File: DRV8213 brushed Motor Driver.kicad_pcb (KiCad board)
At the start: 4 copper layers, 15 x 15 mm, 26 parts, among them J1 Keystone 6102, J10 Precidip 852-10-004-20-001101, J11 Precidip 852-10-004-20-001101, J2 Keystone 6102, J3 Keystone 6100, J4 Keystone 6100, J5 Keystone 6102, J6 Keystone 6102, J7 Keystone 6100, J8 Keystone 6100, J9 JST PH 2mm horizontal, U1 DRV8213RTER, U2 LP2981-3.3

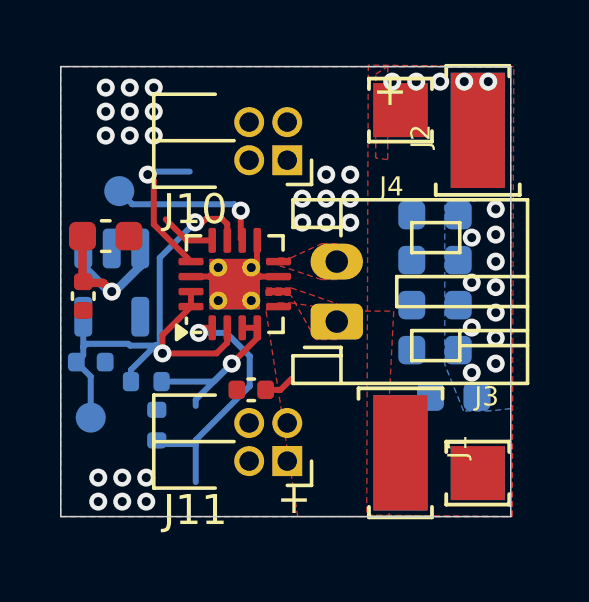
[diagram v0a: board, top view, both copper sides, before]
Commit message: Relayout with new components
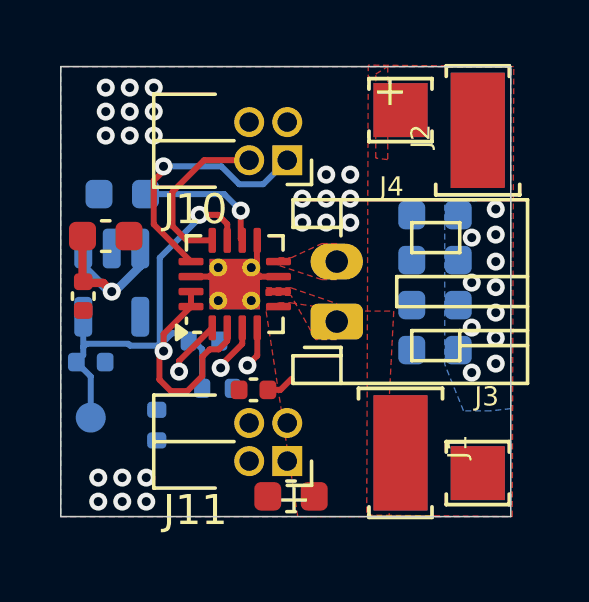
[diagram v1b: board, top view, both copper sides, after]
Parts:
- removed TP1: tinrush, TestPoint:TestPoint_Pad_D1.0mm
- added C10: 33nF, Capacitor_SMD:C_0603_1608Metric, B.Cu at (165.8, 98.5)
- added R3: 10k, Resistor_SMD:R_0402_1005Metric, B.Cu at (168.6, 103.3)
- C5: moved to F.Cu
- moved C5 6.36 mm to (171.5, 108.5)
- moved R1 2.39 mm to (169.0, 104.9)
- moved C6 0.07 mm to (170.2, 105.0)
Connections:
- J11 pad 2: ADC-A -> Stall
- R1 pad 2: Fault -> Stall
- U1 pad 3: Fault -> Stall
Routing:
- net ADC-A: track 8.94 -> 2.09 mm
- net Fault: track 6.54 -> 1.39 mm
- net PWM-B: track 1.84 -> 5.66 mm
- net +3.3V: track 19.8 -> 23.5 mm
- net PWM-A: track 4.94 -> 8.53 mm
- net Stall: track 0.00 -> 1.63 mm, vias 0 -> 1
- net Net-(U1-TINRUSH): track 5.33 -> 4.42 mm
- net VDD: track 7.51 -> 7.43 mm, vias 17 -> 12

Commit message: Finished reroute
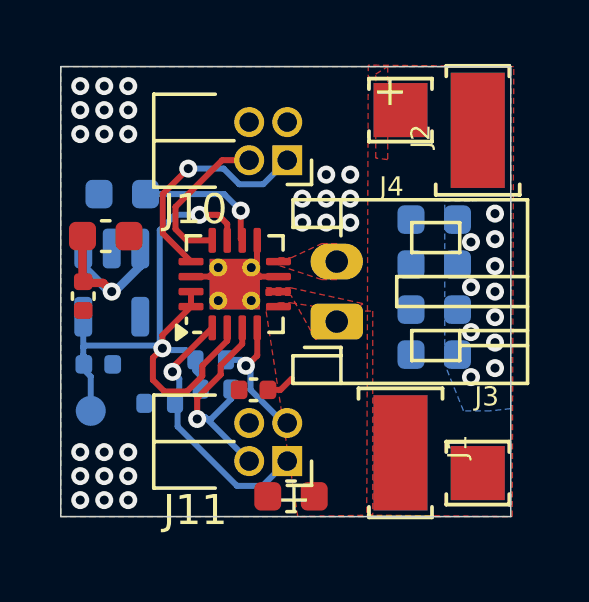
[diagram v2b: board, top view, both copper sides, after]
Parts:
- moved R2 0.73 mm to (167.1, 105.4), turned to 180 degrees
- moved R3 0.66 mm to (168.8, 104.0)
- moved C9 0.26 mm to (165.1, 104.1)
- moved TP2 0.23 mm to (164.8, 105.7)
- moved C1 0.15 mm to (176.2, 99.3)
- moved C2 0.15 mm to (176.2, 102.3)
- moved C3 0.15 mm to (176.2, 100.8)
- moved C4 0.15 mm to (176.2, 103.8)
- moved R1 0.06 mm to (169.0, 105.0)
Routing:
- net ADC-A: track 2.09 -> 8.93 mm
- net Stall: track 1.63 -> 7.74 mm
- net Fault: track 1.39 -> 4.81 mm
- net PWM-A: track 8.53 -> 7.69 mm
- net +3.3V: track 23.5 -> 22.8 mm
- net GNDPWR: vias 23 -> 26
